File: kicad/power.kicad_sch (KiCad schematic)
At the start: 102 parts, among them U1 AP3211, U30 TPS53667RTAR

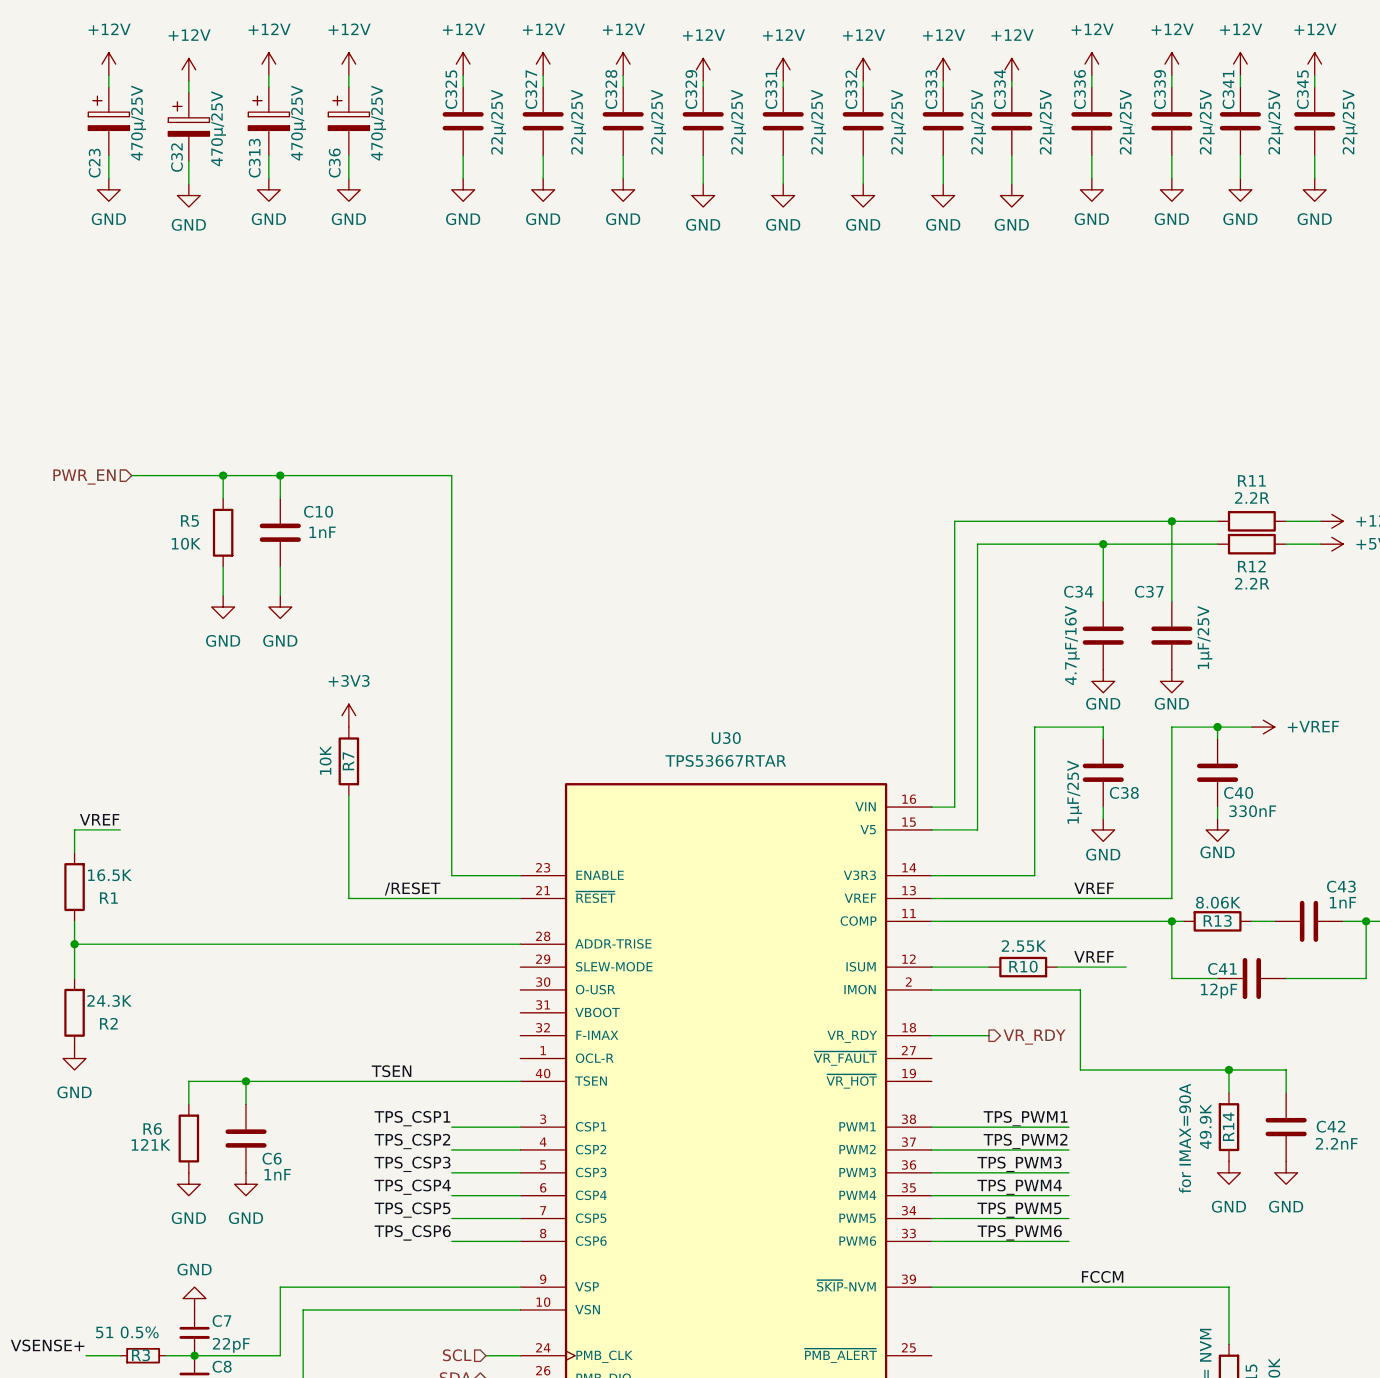
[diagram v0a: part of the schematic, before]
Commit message: final update
Version 1.0 : working as expected, 14TH/s
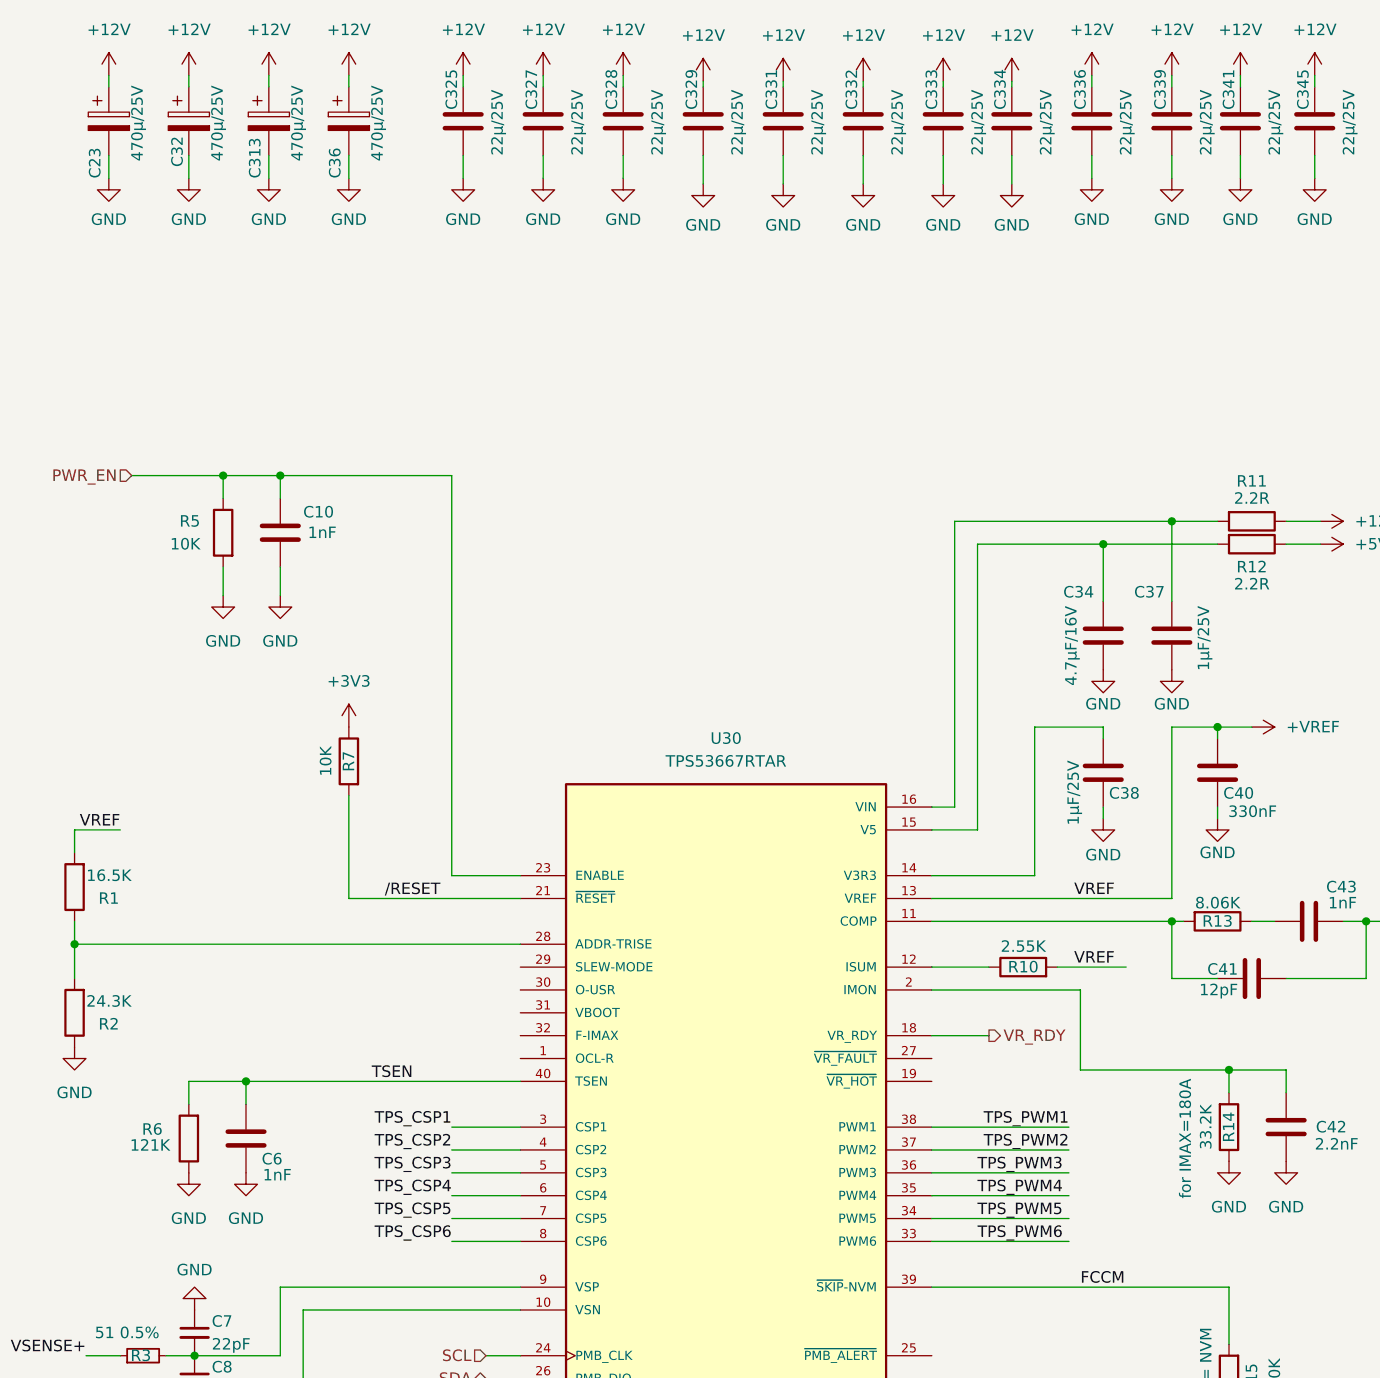
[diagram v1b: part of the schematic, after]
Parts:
- C10, C43, C6: P/N LCSC (none) -> C106244
- C11, C15, C16, C18, C3, C304, C305, C306, C307, C308, C309, C346, C349, C352, C355, C357, C360, C363, C365, C367, C368, C370, C372, C5, C56, C58, C60, C62, C64, C67: P/N LCSC (none) -> C528969
- C12, C14, C28, C29, C30, C31, C33, C35, C39, C44, C45, C46, C47, C48, C49, C50, C51, C52, C53, C54: P/N LCSC (none) -> C15008
- C13: P/N LCSC (none) -> C6119887
- C23, C313, C32, C36: P/N LCSC (none) -> C4054389
- C325, C327, C328, C329, C331, C332, C333, C334, C336, C339, C341, C345, C57: P/N LCSC (none) -> C52306
- C34: P/N LCSC (none) -> C22399642
- C37, C38: P/N LCSC (none) -> C344171
- C40: P/N LCSC (none) -> C73142
- C41: P/N LCSC (none) -> C20218205
- C42: P/N LCSC (none) -> C3907092
- C55: P/N LCSC (none) -> C1710
- C7, C9: P/N LCSC (none) -> C1804
- C8: P/N LCSC (none) -> C3897824
- D2: P/N LCSC (none) -> C96234
- L1: P/N LCSC (none) -> C703747
- R1, R9: P/N LCSC (none) -> C35929
- R10: P/N LCSC (none) -> C2933383
- R11, R12: P/N LCSC (none) -> C17521
- R13: P/N LCSC (none) -> C2933501
- R14: value 49.9K -> 33.2K; Manufacturer CR0805-FX-4992ELF -> RMCF0805FT33K2; P/N LCSC (none) -> C3016779; P/N MOUSER 652-CR0805FX-4992ELF -> 708-RMCF0805FT33K2
- R15: P/N LCSC (none) -> C149504
- R2: P/N LCSC (none) -> C17569
- R3, R4: P/N LCSC (none) -> C868849
- R5, R7: P/N LCSC (none) -> C84376
- R6: P/N LCSC (none) -> C17438
- R8: P/N LCSC (none) -> C17846
- U1: P/N LCSC (none) -> C154863
- U30: P/N LCSC (none) -> C702270
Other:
- note added: "for IMAX=180A"
- note removed: "for IMAX=90A"
- moved on the sheet: C32
